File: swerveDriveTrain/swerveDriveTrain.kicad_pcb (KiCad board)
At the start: 2 copper layers, 41 parts, among them IC1 TCAN3414DR, J1 RJ45, J2 Screw_Terminal_01x02, J3 Conn_01x06_Pin, J4 S6B-PH-K-S_LF__SN_, P1 USB_C_Plug_USB2.0, U2 Teensy4.0

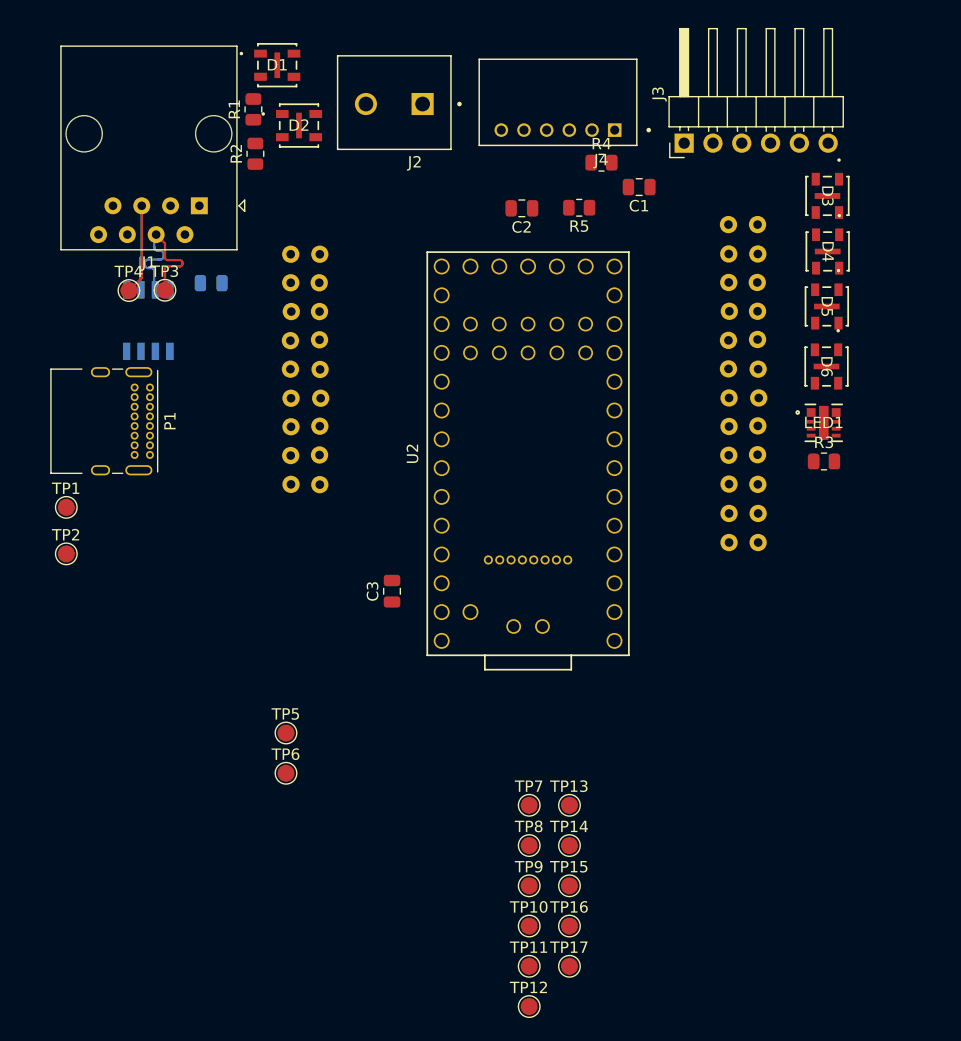
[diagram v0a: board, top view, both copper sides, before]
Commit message: layout and routing for swerve
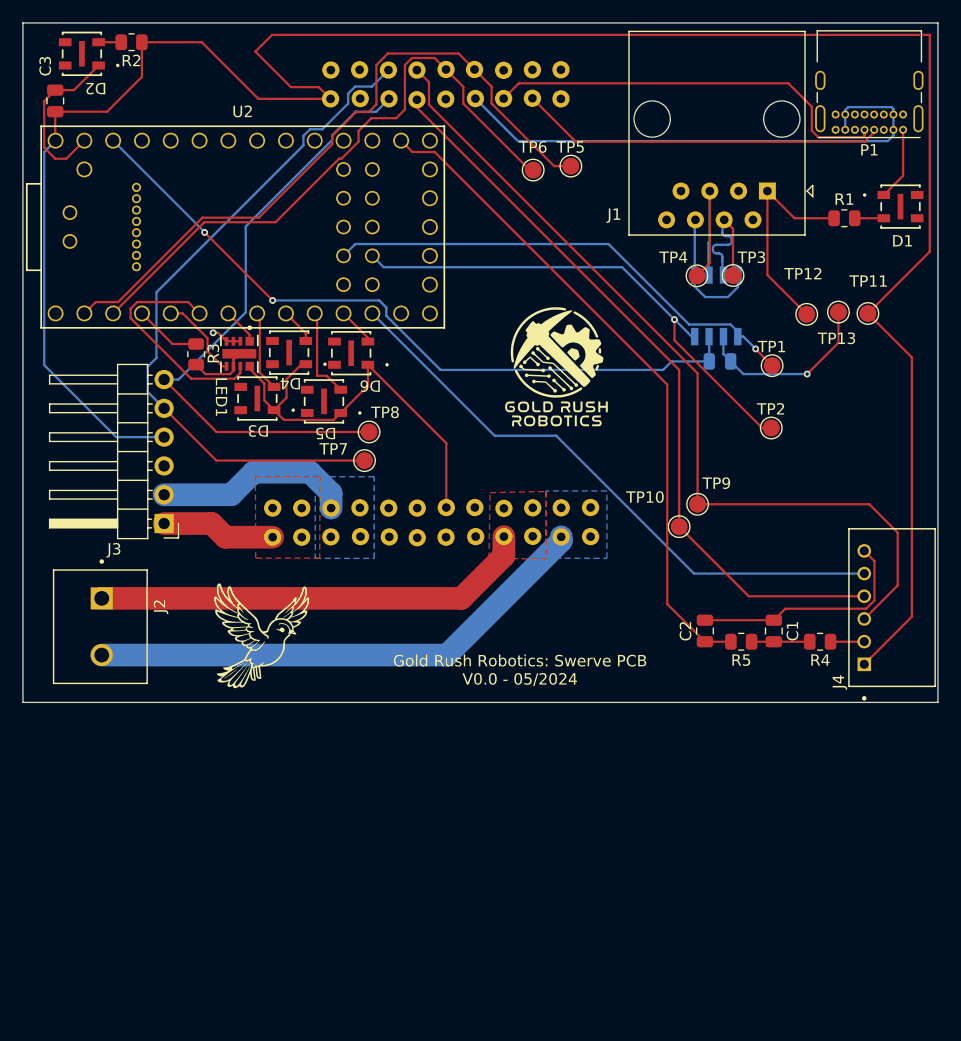
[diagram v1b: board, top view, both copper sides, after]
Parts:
- removed TP14, TP15, TP16, TP17: TestPoint_Probe, TestPoint:TestPoint_Pad_D1.5mm
- added J5: Conn_01x01_Pin, footprints:Logo_Small, F.Cu at (57.7, 42.3)
- added J6: Conn_01x01_Pin, footprints:bird, F.Cu at (31.7, 66.0)
- moved P1 70.2 mm to (88.2, 21.4), turned to 180 degrees
- moved TP12 65.8 mm to (79.8, 37.6)
- moved TP11 64.9 mm to (85.2, 37.6)
- moved TP1 63.5 mm to (76.7, 42.2)
- moved TP2 63.2 mm to (76.6, 47.7)
- moved TP6 57.5 mm to (55.6, 24.9)
- moved J2 57.3 mm to (13.3, 60.2), turned to -90 degrees
- moved J3 56.8 mm to (23.1, 56.1), turned to 180 degrees
- moved D1 56.4 mm to (88.0, 28.2)
- moved R3 56.2 mm to (25.9, 41.2), turned to -90 degrees
- moved TP5 56.0 mm to (59.0, 24.6)
- moved D3 53.4 mm to (31.3, 45.1), turned to 180 degrees
- moved R1 53.0 mm to (83.1, 29.2), turned to 0 degrees
- moved C3 52.5 mm to (13.5, 18.8)
- moved LED1 51.9 mm to (29.7, 41.1), turned to -90 degrees
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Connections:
- net CANH renamed CANP
- net CANL renamed CANN
- C3 pad 1: GND -> +5V
- C3 pad 2: CAN3v3 -> GND
- C4 pad 1: +5V -> GND
- C4 pad 2: GND -> CAN3v3
- TP11 pad 1: S1 -> +5V
- TP12 pad 1: S2 -> +12V
- TP13 pad 1: S3 -> GND
- U1 pad 11: S2 -> TXD
- U1 pad 9: S1 -> RXD
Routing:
- net +5V: track 0.00 -> 196.2 mm
- net GND: track 0.00 -> 122.4 mm, vias 0 -> 2
- net ENC2A: track 0.00 -> 76.1 mm
- net ENC2B: track 0.00 -> 66.1 mm
- net CAN3v3: track 0.00 -> 64.0 mm, vias 0 -> 2
- net ENC1A: track 0.00 -> 60.3 mm
- net TXD: track 0.00 -> 59.9 mm
- net ABSA: track 0.00 -> 58.7 mm
- net ENC1B: track 0.00 -> 54.8 mm
- net RXD: track 0.00 -> 54.2 mm
- net ENC2I: track 0.00 -> 52.9 mm
- net VBUS: track 0.00 -> 47.1 mm
- net M2A: track 0.00 -> 45.0 mm
- net CRX: track 0.00 -> 44.9 mm, vias 0 -> 1
- net CTX: track 0.00 -> 43.0 mm, vias 0 -> 1
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- added copper zone on In1.Cu, net +12V
- added copper zone on In1.Cu, net GND
- added copper zone on In2.Cu, net GND
- added copper zone on F.Cu, net M1A
- added copper zone on B.Cu, net M1B
- added copper zone on B.Cu, net M2A
- added copper zone on F.Cu, net M2B
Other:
- board outline added: 80.7 x 59.9 mm
- copper layers 2 -> 4
- board text added: "Gold Rush Robotics: Swerve PCB V0.0 - 05/2024"

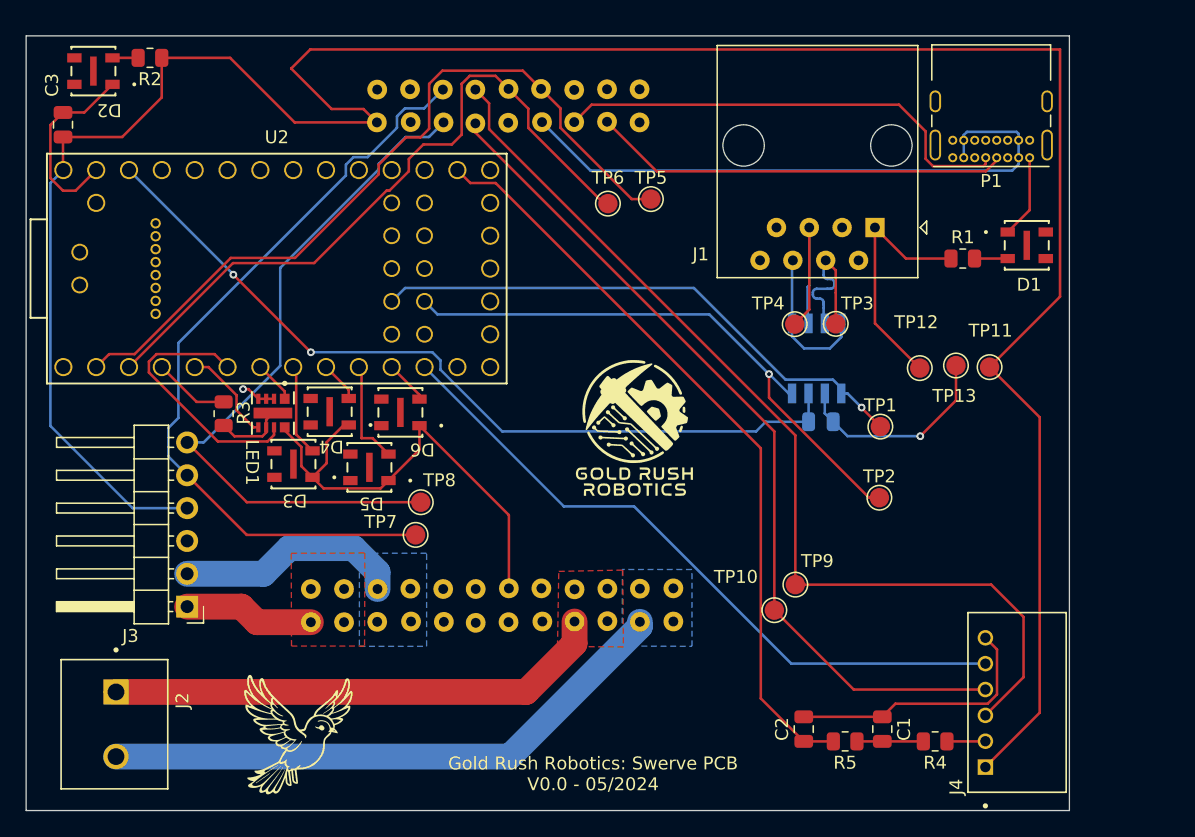
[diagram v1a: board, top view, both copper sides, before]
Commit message: update schematic and make a blank pcb layout for testing
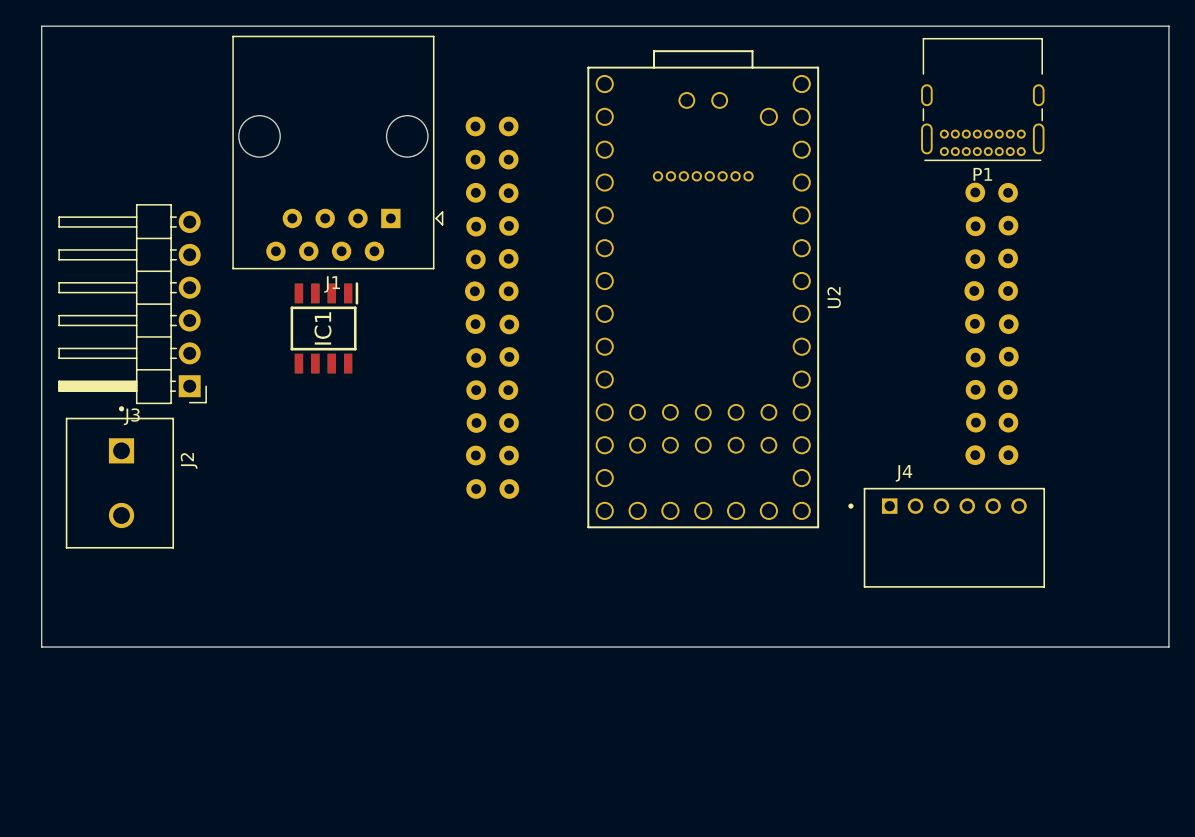
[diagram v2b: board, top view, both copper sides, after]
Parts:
- removed C1, C2: 1 uF, Capacitor_SMD:C_0805_2012Metric
- removed C3, C4: 0.1 uF, Capacitor_SMD:C_0805_2012Metric
- removed D1, D2, D3, D4, D5, D6: LED, GreenLED:LED_CREE_MLXXXX
- removed J5: Conn_01x01_Pin, footprints:Logo_Small
- removed J6: Conn_01x01_Pin, footprints:bird
- removed LED1: 599-2310-427F, footprints:599-2310_DIA
- removed R1: 25, Resistor_SMD:R_0805_2012Metric
- removed R2: 5, Resistor_SMD:R_0805_2012Metric
- removed R3: 15, Resistor_SMD:R_0805_2012Metric
- removed R4, R5: 10k, Resistor_SMD:R_0805_2012Metric
- removed TP1, TP10, TP11, TP12, TP13, TP2, TP3, TP4, TP5, TP6, TP7, TP8, TP9: TestPoint_Probe, TestPoint:TestPoint_Pad_D1.5mm
- IC1: moved to F.Cu
- moved IC1 38.2 mm to (33.6, 34.6), turned to -90 degrees
- moved J1 37.5 mm to (38.8, 26.1)
- moved U2 33.1 mm to (63.0, 32.2), turned to -90 degrees
- moved U1 27.2 mm to (67.6, 27.7), turned to 180 degrees
- moved J2 18.7 mm to (13.8, 41.5)
- moved J3 17.1 mm to (23.3, 39.0)
- moved J4 15.4 mm to (82.4, 48.3), turned to 0 degrees
- moved P1 0.81 mm to (87.6, 20.9)
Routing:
- net +5V: track 196.2 -> 0.00 mm
- net GND: track 122.4 -> 0.00 mm, vias 2 -> 0
- net ENC2A: track 76.1 -> 0.00 mm
- net ENC2B: track 66.1 -> 0.00 mm
- net CAN3v3: track 64.0 -> 0.00 mm, vias 2 -> 0
- net ENC1A: track 60.3 -> 0.00 mm
- net TXD: track 59.9 -> 0.00 mm
- net ABSA: track 58.7 -> 0.00 mm
- net ENC1B: track 54.8 -> 0.00 mm
- net RXD: track 54.2 -> 0.00 mm
- net ENC2I: track 52.9 -> 0.00 mm
- net VBUS: track 47.1 -> 0.00 mm
- net M2A: track 45.0 -> 0.00 mm
- net CRX: track 44.9 -> 0.00 mm, vias 1 -> 0
- net CTX: track 43.0 -> 0.00 mm, vias 1 -> 0
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- removed copper zone on In1.Cu, net +12V
- removed copper zone on In1.Cu, net GND
- removed copper zone on In2.Cu, net GND
- removed copper zone on F.Cu, net M1A
- removed copper zone on B.Cu, net M1B
- removed copper zone on B.Cu, net M2A
- removed copper zone on F.Cu, net M2B
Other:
- board size 80.7 x 59.9 mm -> 87.2 x 48 mm
- board text removed: "Gold Rush Robotics: Swerve PCB V0.0 - 05/2024"

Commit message: work on the swerve drive
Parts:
- IC1, J3: moved to B.Cu
- moved J2 102.3 mm to (39.7, 140.5), turned to 0 degrees
- moved J3 95.3 mm to (16.9, 134.1), turned to -90 degrees
- moved U1 90.3 mm to (25.1, 107.4), turned to -90 degrees
- moved U2 81.4 mm to (33.1, 108.0), turned to 0 degrees
- moved P1 72.1 mm to (25.1, 56.8), turned to -90 degrees
- moved J4 57.1 mm to (27.9, 31.4), turned to 90 degrees
- moved J1 45.8 mm to (29.8, 71.0), turned to -90 degrees
- moved IC1 42.3 mm to (20.5, 74.8), turned to 0 degrees
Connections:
- J1 pad 4: CANP -> GND
- J1 pad 5: CANN -> GND
- J1 pad 7: GND -> CANP
- J1 pad 8: GND -> CANN
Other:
- board size 87.2 x 48 mm -> 82.2 x 124.9 mm

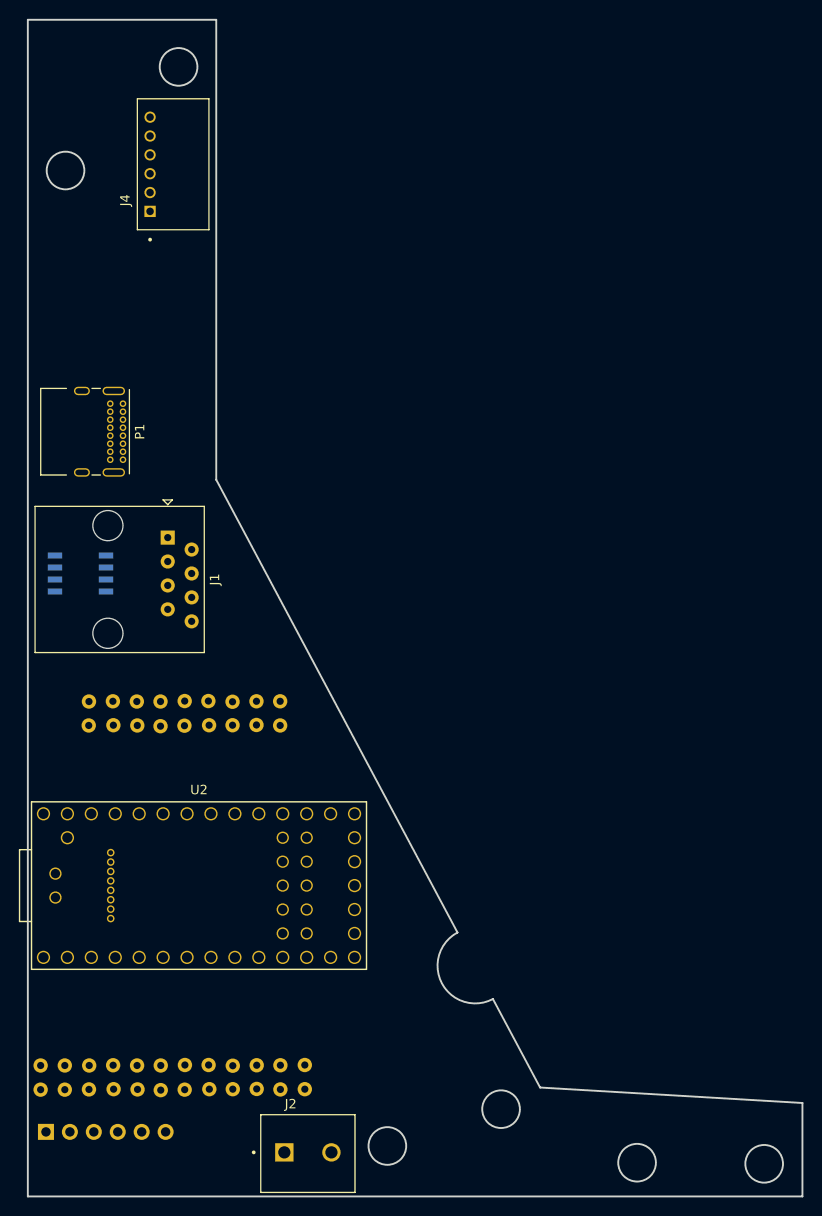
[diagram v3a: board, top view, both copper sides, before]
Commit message: switched motor drivers out schematic and footprint
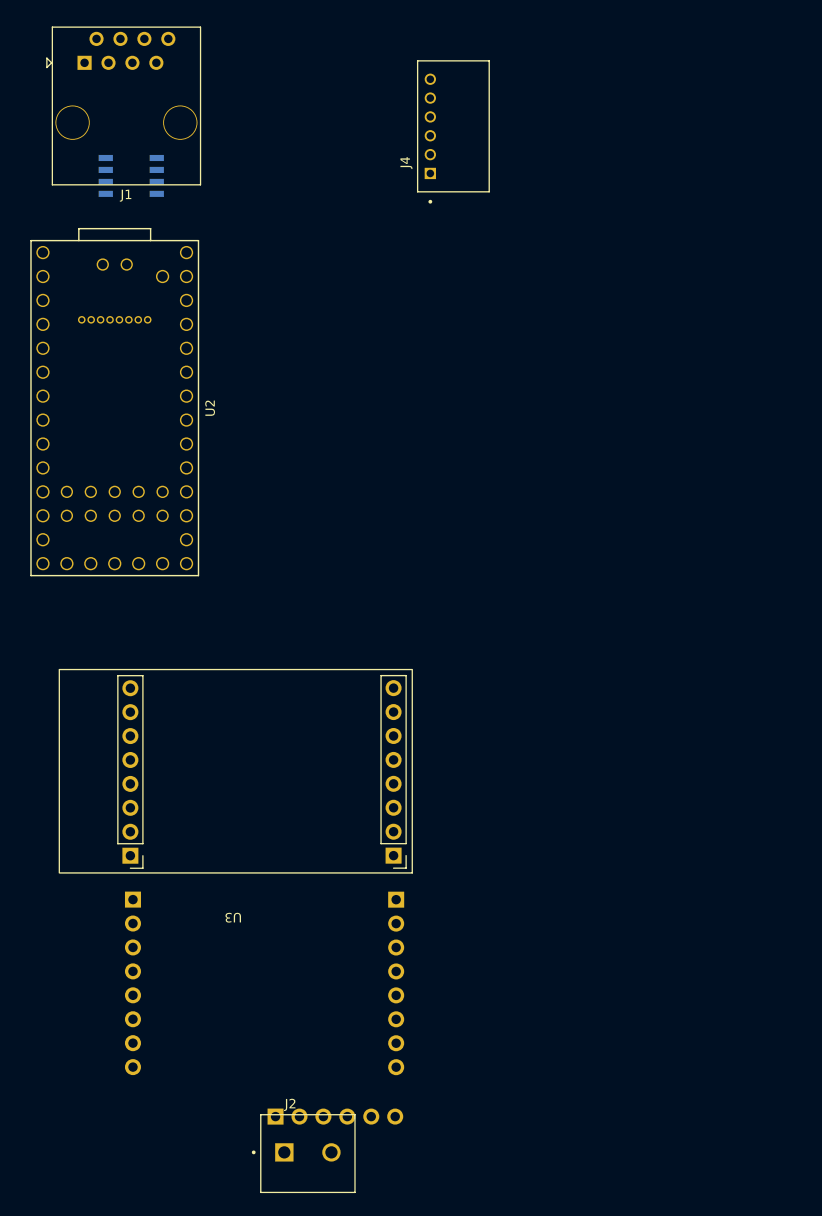
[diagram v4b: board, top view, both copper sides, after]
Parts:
- removed P1: USB_C_Plug_USB2.0, Connector_USB:USB_C_Receptacle_GCT_USB4085
- added U3: ~, footprints:G218v17, F.Cu at (36.8, 110.8)
- J1: footprint Connector_RJ:RJ45_Amphenol_54602-x08_Horizontal -> Connector_RJ:RJ45_OST_PJ012-8P8CX_Vertical
- U1: footprint Custom:roboclaw -> footprints:G218v17
- moved U2 51.5 mm to (24.2, 57.3), turned to -90 degrees
- moved J1 51.2 mm to (21.0, 20.6), turned to 0 degrees
- moved IC1 42.5 mm to (25.9, 32.6)
- moved J4 30.0 mm to (57.7, 27.4)
- moved J3 24.4 mm to (41.2, 132.5)
- moved U1 12.6 mm to (37.0, 103.4), turned to 180 degrees
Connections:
- U1 pad 1: unconnected-(U1-LB_IN-Pad1) -> DIR1
- U1 pad 10: GND -> M1A
- U1 pad 11: TXD -> M1A
- U1 pad 12: VBUS -> M1B
- U1 pad 13: S3 -> M1B
- U1 pad 14: DP -> +12V
- U1 pad 15: S4 -> +12V
- U1 pad 2: +5V -> PWM1
- U1 pad 3: GND -> unconnected-(U1-SLP-Pad3)
- U1 pad 4: GND -> FLTM1
- U1 pad 5: ENC1A -> CSM1
- U1 pad 7: ENC2A -> unconnected-(U1-VM-Pad7)
- U1 pad 8: ENC2B -> GND
- U1 pad 9: RXD -> GND
- U2 pad 10: LED3 -> ENC1A
- U2 pad 11: LED4 -> ENC1B
- U2 pad 13: unconnected-(U2-11_MOSI_CTX1-Pad13) -> ENC2A
- U2 pad 14: unconnected-(U2-12_MISO_MQSL-Pad14) -> ENC2B
- U2 pad 2: TXD -> PWM1
- U2 pad 22: unconnected-(U2-15_A1_RX3_SPDIF_IN-Pad22) -> CSM1
- U2 pad 23: unconnected-(U2-16_A2_RX4_SCL1-Pad23) -> CSM2
- U2 pad 25: unconnected-(U2-18_A4_SDA0-Pad25) -> DIR1
- U2 pad 26: unconnected-(U2-19_A5_SCL0-Pad26) -> DIR2
- U2 pad 27: unconnected-(U2-20_A6_TX5_LRCLK1-Pad27) -> FLTM1
- U2 pad 28: unconnected-(U2-21_A7_RX5_BCLK1-Pad28) -> FLTM2
- U2 pad 3: RXD -> PWM2
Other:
- board outline removed

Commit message: work on fitting into footprint
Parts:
- added C1: 1 uF, Capacitor_SMD:C_0805_2012Metric, F.Cu at (85.1, 56.2)
- added C2: 1 uF, Capacitor_SMD:C_0805_2012Metric, F.Cu at (85.1, 59.2)
- added C3: 0.1 uF, Capacitor_SMD:C_0805_2012Metric, F.Cu at (85.1, 62.3)
- added C4: 0.1 uF, Capacitor_SMD:C_0805_2012Metric, F.Cu at (61.0, 112.1)
- added D1: LED, GreenLED:LED_CREE_MLXXXX, F.Cu at (108.8, 69.2)
- added D2: LED, GreenLED:LED_CREE_MLXXXX, F.Cu at (108.8, 74.3)
- added D3: LED, GreenLED:LED_CREE_MLXXXX, F.Cu at (108.8, 79.5)
- added D4: LED, GreenLED:LED_CREE_MLXXXX, F.Cu at (108.8, 84.6)
- added L1: ~, footprints:Logo_Small, F.Cu at (100.6, 92.3)
- added L2: ~, footprints:bird, F.Cu at (110.3, 91.6)
- added LED1: 599-2310-427F, footprints:599-2310_DIA, F.Cu at (85.8, 69.1)
- added R1: 25, Resistor_SMD:R_0805_2012Metric, F.Cu at (80.6, 56.2)
- added R2: 5, Resistor_SMD:R_0805_2012Metric, F.Cu at (80.6, 59.2)
- added R3: 15, Resistor_SMD:R_0805_2012Metric, F.Cu at (113.2, 71.8)
- added R4: 10k, Resistor_SMD:R_0805_2012Metric, F.Cu at (80.6, 65.1)
- added R5: 10k, Resistor_SMD:R_0805_2012Metric, F.Cu at (80.6, 68.0)
- added R6: R, Resistor_SMD:R_0805_2012Metric_Pad1.20x1.40mm_HandSolder, F.Cu at (78.0, 77.2)
- added R7: R, Resistor_SMD:R_0805_2012Metric_Pad1.20x1.40mm_HandSolder, F.Cu at (78.0, 80.2)
- added TP1: TestPoint_Probe, TestPoint:TestPoint_Pad_D1.5mm, F.Cu at (110.1, 46.5)
- added TP10: TestPoint_Probe, TestPoint:TestPoint_Pad_D1.5mm, F.Cu at (113.7, 60.7)
- added TP11: TestPoint_Probe, TestPoint:TestPoint_Pad_D1.5mm, F.Cu at (117.2, 46.5)
- added TP12: TestPoint_Probe, TestPoint:TestPoint_Pad_D1.5mm, F.Cu at (117.2, 50.0)
- added TP13: TestPoint_Probe, TestPoint:TestPoint_Pad_D1.5mm, F.Cu at (117.2, 53.6)
- added TP2: TestPoint_Probe, TestPoint:TestPoint_Pad_D1.5mm, F.Cu at (110.1, 50.0)
- added TP3: TestPoint_Probe, TestPoint:TestPoint_Pad_D1.5mm, F.Cu at (110.1, 53.6)
- added TP4: TestPoint_Probe, TestPoint:TestPoint_Pad_D1.5mm, F.Cu at (110.1, 57.1)
- added TP5: TestPoint_Probe, TestPoint:TestPoint_Pad_D1.5mm, F.Cu at (110.1, 60.7)
- added TP6: TestPoint_Probe, TestPoint:TestPoint_Pad_D1.5mm, F.Cu at (113.7, 46.5)
- added TP7: TestPoint_Probe, TestPoint:TestPoint_Pad_D1.5mm, F.Cu at (113.7, 50.0)
- added TP8: TestPoint_Probe, TestPoint:TestPoint_Pad_D1.5mm, F.Cu at (113.7, 53.6)
- added TP9: TestPoint_Probe, TestPoint:TestPoint_Pad_D1.5mm, F.Cu at (113.7, 57.1)
- J3: moved to F.Cu
- moved J1 115.2 mm to (57.8, 129.8)
- moved IC1 96.1 mm to (63.6, 121.0), turned to -60 degrees
- moved J2 55.7 mm to (19.6, 88.6), turned to -90 degrees
- moved U1 43.6 mm to (41.4, 146.8), turned to 0 degrees
- moved U3 14.1 mm to (38.3, 96.8), turned to 0 degrees
- moved J4 11.9 mm to (45.9, 26.2)
- moved U2 4.95 mm to (28.6, 55.1)
- moved J3 4.66 mm to (45.9, 133.0)
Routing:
- net +5V: track 0.00 -> 109.8 mm, vias 0 -> 2
- net CAN3v3: track 0.00 -> 85.6 mm, vias 0 -> 1
- net CTX: track 0.00 -> 74.7 mm
- net CRX: track 0.00 -> 70.5 mm
- net M2B: track 0.00 -> 43.2 mm
- net M2A: track 0.00 -> 32.8 mm
- net M1B: track 0.00 -> 13.0 mm
- net M1A: track 0.00 -> 9.03 mm
- net CANP: track 0.00 -> 6.54 mm
- net CANN: track 0.00 -> 4.70 mm
- added copper zone on F.Cu, net +12V
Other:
- board outline added: 55 x 125.6 mm
